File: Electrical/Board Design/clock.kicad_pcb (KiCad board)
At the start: 2 copper layers, 133.3 x 50.8 mm, 59 parts, among them CON1 AVR-ISP-6, CON2 USB-MICRO-B, IC1 ATTINY84A-SS, P1 CONN_6, P2 CONN_2, P3 CONN_2, P4 CONN_2, P5 CONN_2, P6 CONN_2, P7 CONN_2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

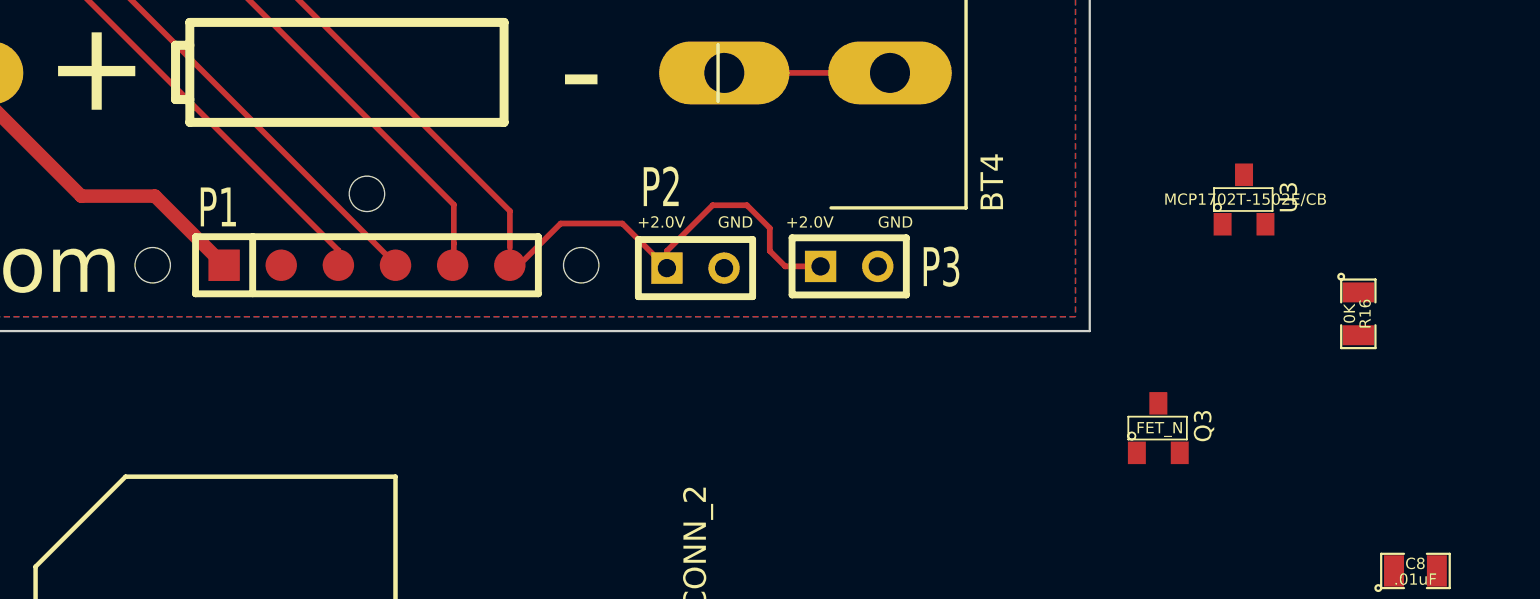
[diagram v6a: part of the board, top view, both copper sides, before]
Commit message: updated test pad foot print and also some transistors
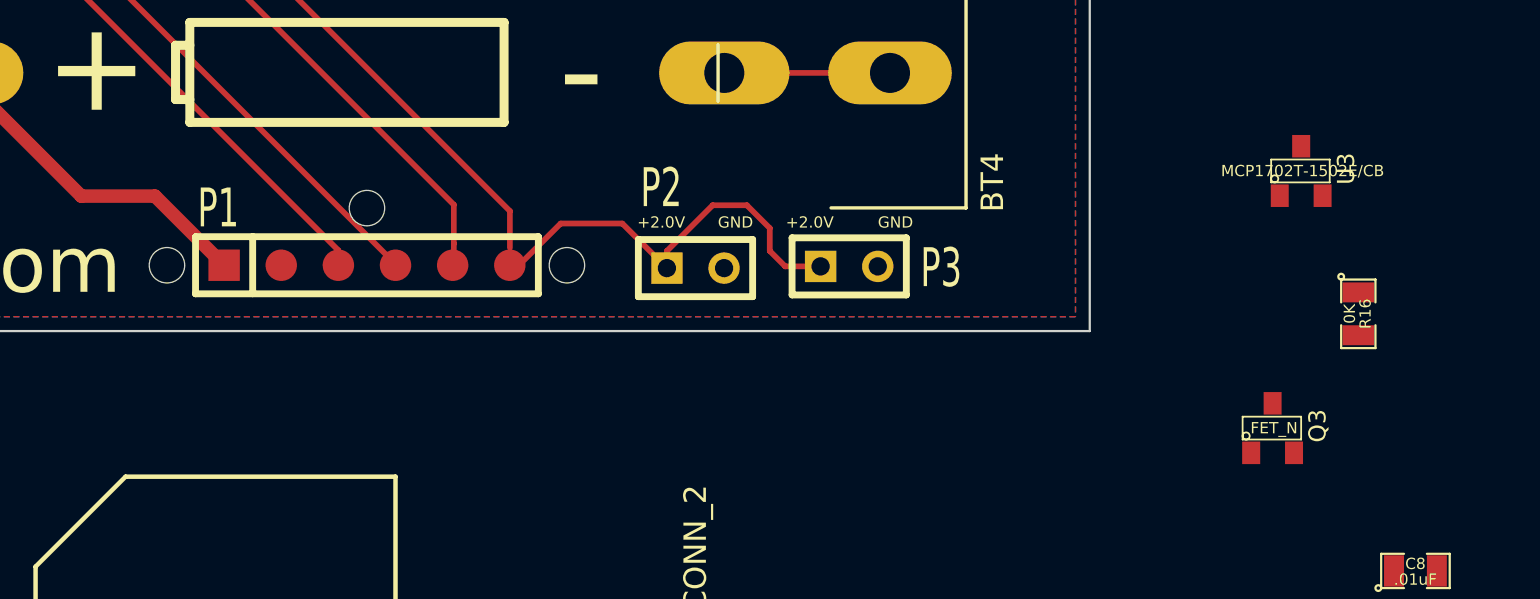
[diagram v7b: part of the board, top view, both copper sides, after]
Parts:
- moved Q3 5.08 mm to (199.4, 128.3)
- moved U3 2.84 mm to (200.7, 116.8)
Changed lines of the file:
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@@
 (kicad_pcb (version 3) (host pcbnew "(2013-07-07 BZR 4022)-stable")
   (general
-    (links 118)
-    (no_connects 40)
-    (area 57.861999 73.101999 191.312001 124.007001)
+    (links 120)
+    (no_connects 62)
+    (area 44.831088 64.333001 247.248333 153.332111)
     (thickness 1.6)
     (drawings 69)
@@
     (mod_text_size 1 1)
     (mod_text_width 0.15)
-    (pad_size 4 3)
+    (pad_size 0.8001 1.00076)
     (pad_drill 0)
     (pad_to_mask_clearance 0)
@@
     )
   )
-  (module SIL-6_s (layer F.Cu)
-    (at 159.131 121.031)
-    (descr "keyed connector")
-    (tags "CONN DEV")
-    (fp_text reference P1 (at -6.61 -2.528) (layer F.SilkS)
-      (effects (font (size 1.72974 1.08712) (thickness 0.3048)))
-    )
-    (fp_text value CONN_6 (at 3.931 -2.528) (layer F.SilkS) hide
-      (effects (font (size 1.524 1.016) (thickness 0.254)))
-    )
-    (fp_line (start -7.62 1.27) (end -7.62 -1.27) (layer F.SilkS) (width 0.3048))
-    (fp_line (start -7.62 -1.27) (end 7.62 -1.27) (layer F.SilkS) (width 0.3048))
-    (fp_line (start 7.62 -1.27) (end 7.62 1.27) (layer F.SilkS) (width 0.3048))
-    (fp_line (start 7.62 1.27) (end -7.62 1.27) (layer F.SilkS) (width 0.3048))
-    (fp_line (start -5.08 1.27) (end -5.08 -1.27) (layer F.SilkS) (width 0.3048))
-    (pad 1 smd rect (at -6.35 0) (size 1.397 1.397)
-      (layers F.Cu F.Paste F.Mask)
-      (net 5 "/BATTERY POWER")
-    )
-    (pad 2 smd circle (at -3.81 0) (size 1.397 1.397)
-      (layers F.Cu F.Paste F.Mask)
-      (net 12 GND)
-    )
-    (pad 3 smd circle (at -1.27 0) (size 1.397 1.397)
-      (layers F.Cu F.Paste F.Mask)
-      (net 9 /MINUTES)
-    )
-    (pad 4 smd circle (at 1.27 0) (size 1.397 1.397)
-      (layers F.Cu F.Paste F.Mask)
-      (net 6 /HOURS)
-    )
-    (pad 5 smd circle (at 3.81 0) (size 1.397 1.397)
-      (layers F.Cu F.Paste F.Mask)
-      (net 10 "/MODE SELECT")
-    )
-    (pad 6 smd circle (at 6.35 0) (size 1.397 1.397)
-      (layers F.Cu F.Paste F.Mask)
-      (net 31 VCC)
-    )
-    (pad "" np_thru_hole oval (at 9.525 0) (size 1.5748 1.5748) (drill 1.5748)
-      (layers *.Cu *.Mask F.SilkS)
-    )
-    (pad 1 np_thru_hole oval (at -9.525 0) (size 1.5748 1.5748) (drill 1.5748)
-      (layers *.Cu *.Mask F.SilkS)
-      (net 5 "/BATTERY POWER")
-    )
-    (pad "" np_thru_hole oval (at 0 -3.175) (size 1.5748 1.5748) (drill 1.5748)
-      (layers *.Cu *.Mask F.SilkS)
-    )
-  )
   (module bourns_knob (layer B.Cu)
     (at 67.437 80.777004)
@@
   )
   (module SOT23 (layer F.Cu)
-    (at 194.31 128.27)
+    (at 199.39 128.27)
     (tags SOT23)
     (fp_text reference Q3 (at 1.99898 -0.09906 90) (layer F.SilkS)
@@
   )
   (module SOT23 (layer F.Cu)
-    (at 198.12 118.11)
+    (at 200.66 116.84)
     (tags SOT23)
     (fp_text reference U3 (at 1.99898 -0.09906 90) (layer F.SilkS)
@@
     (fp_line (start 1.27 0.508) (end -1.3335 0.508) (layer F.SilkS) (width 0.07874))
     (fp_line (start -1.3335 -0.508) (end 1.27 -0.508) (layer F.SilkS) (width 0.07874))
-    (pad 3 smd rect (at 0 -1.09982) (size 0.8001 1.00076)
-      (layers F.Cu F.Paste F.Mask)
-    )
-    (pad 2 smd rect (at 0.9525 1.09982) (size 0.8001 1.00076)
-      (layers F.Cu F.Paste F.Mask)
-    )
-    (pad 1 smd rect (at -0.9525 1.09982) (size 0.8001 1.00076)
-      (layers F.Cu F.Paste F.Mask)
+    (pad D smd rect (at 0 -1.09982) (size 0.8001 1.00076)
+      (layers F.Cu F.Paste F.Mask)
+      (net 16 N-0000015)
+    )
+    (pad S smd rect (at 0.9525 1.09982) (size 0.8001 1.00076)
+      (layers F.Cu F.Paste F.Mask)
+      (net 12 GND)
+    )
+    (pad G smd rect (at -0.9525 1.09982) (size 0.8001 1.00076)
+      (layers F.Cu F.Paste F.Mask)
+      (net 2 "/ALARM BUZZER")
     )
     (model smd\SOT23_3.wrl
@@
     )
   )
+  (module SIL-6_s (layer F.Cu)
+    (at 159.131 121.031)
+    (descr "keyed connector")
+    (tags "CONN DEV")
+    (fp_text reference P1 (at -6.61 -2.528) (layer F.SilkS)
+      (effects (font (size 1.72974 1.08712) (thickness 0.3048)))
+    )
+    (fp_text value CONN_6 (at 3.931 -2.528) (layer F.SilkS) hide
+      (effects (font (size 1.524 1.016) (thickness 0.254)))
+    )
+    (fp_line (start -7.62 1.27) (end -7.62 -1.27) (layer F.SilkS) (width 0.3048))
+    (fp_line (start -7.62 -1.27) (end 7.62 -1.27) (layer F.SilkS) (width 0.3048))
+    (fp_line (start 7.62 -1.27) (end 7.62 1.27) (layer F.SilkS) (width 0.3048))
+    (fp_line (start 7.62 1.27) (end -7.62 1.27) (layer F.SilkS) (width 0.3048))
+    (fp_line (start -5.08 1.27) (end -5.08 -1.27) (layer F.SilkS) (width 0.3048))
+    (pad 1 smd rect (at -6.35 0) (size 1.397 1.397)
+      (layers F.Cu F.Paste F.Mask)
+      (net 5 "/BATTERY POWER")
+    )
+    (pad 2 smd circle (at -3.81 0) (size 1.397 1.397)
+      (layers F.Cu F.Paste F.Mask)
+      (net 12 GND)
+    )
+    (pad 3 smd circle (at -1.27 0) (size 1.397 1.397)
+      (layers F.Cu F.Paste F.Mask)
+      (net 9 /MINUTES)
+    )
+    (pad 4 smd circle (at 1.27 0) (size 1.397 1.397)
+      (layers F.Cu F.Paste F.Mask)
+      (net 6 /HOURS)
+    )
+    (pad 5 smd circle (at 3.81 0) (size 1.397 1.397)
+      (layers F.Cu F.Paste F.Mask)
+      (net 10 "/MODE SELECT")
+    )
+    (pad 6 smd circle (at 6.35 0) (size 1.397 1.397)
+      (layers F.Cu F.Paste F.Mask)
+      (net 31 VCC)
+    )
+    (pad "" np_thru_hole oval (at 8.89 0) (size 1.5748 1.5748) (drill 1.5748)
+      (layers *.Cu *.Mask F.SilkS)
+    )
+    (pad "" np_thru_hole oval (at -8.89 0) (size 1.5748 1.5748) (drill 1.5748)
+      (layers *.Cu *.Mask F.SilkS)
+    )
+    (pad "" np_thru_hole oval (at 0 -2.54) (size 1.5748 1.5748) (drill 1.5748)
+      (layers *.Cu *.Mask F.SilkS)
+    )
+  )

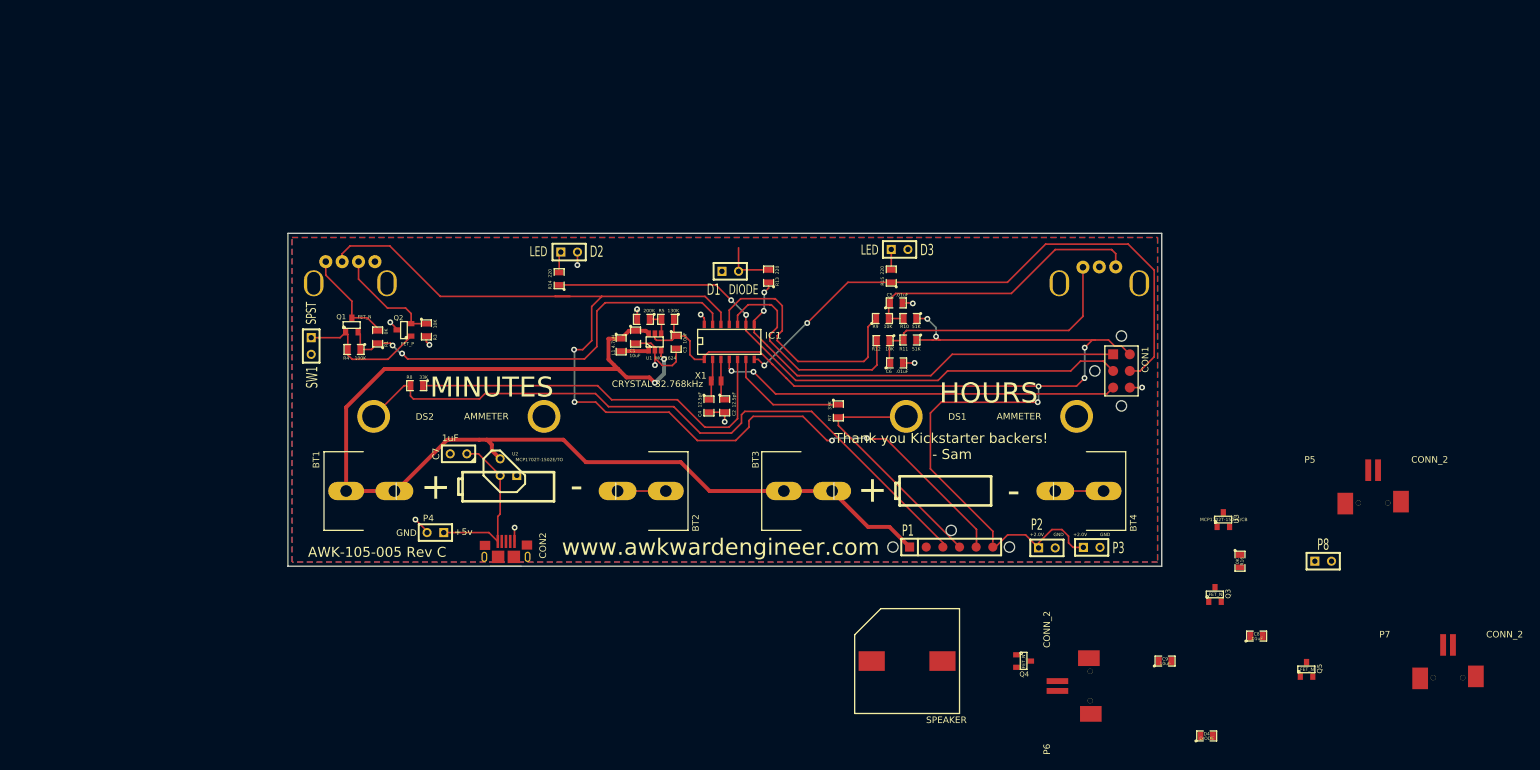
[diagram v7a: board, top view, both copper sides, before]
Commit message: reorganized board layout, but haven't fully wired
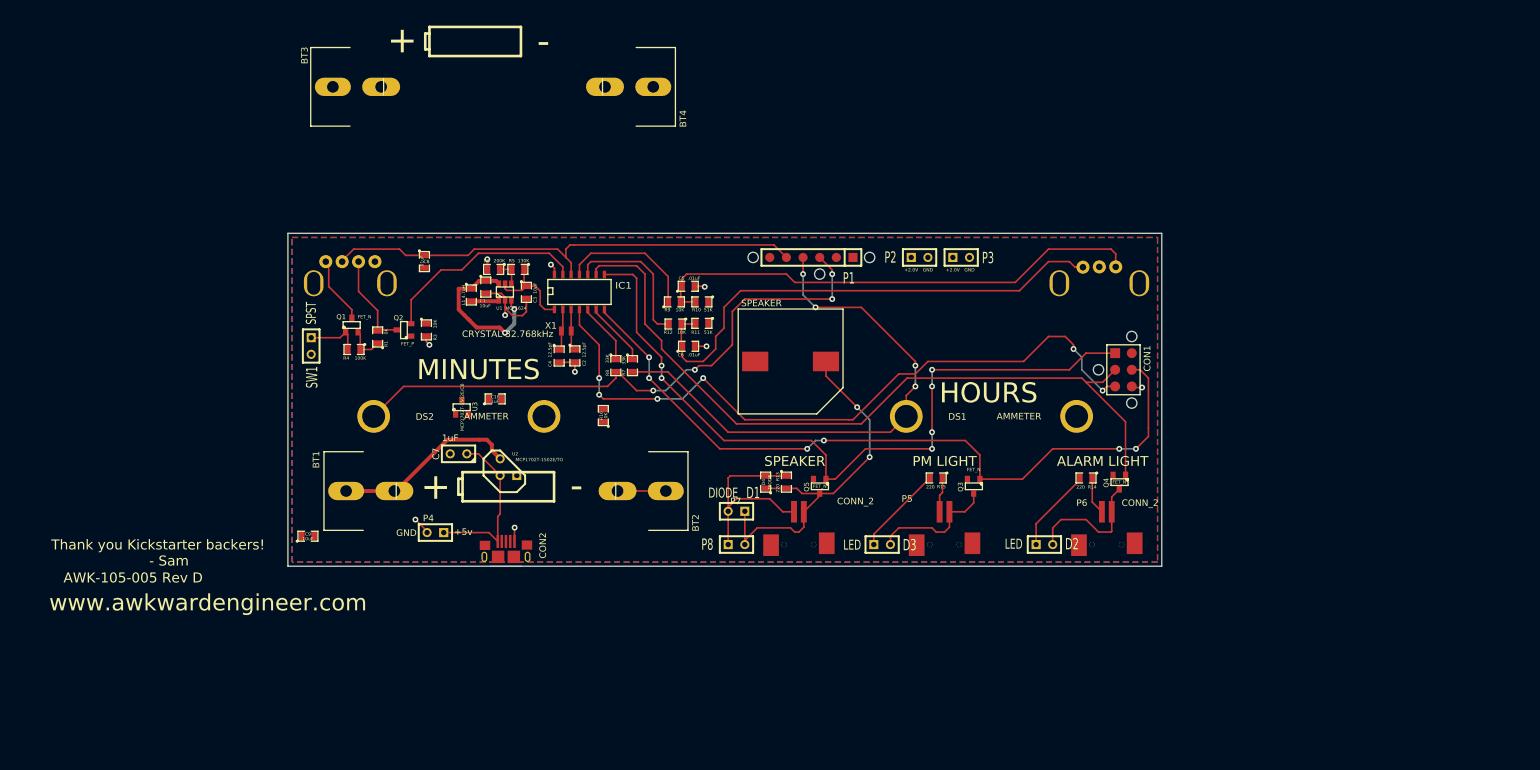
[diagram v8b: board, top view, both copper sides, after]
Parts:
- added C10: 1uF, SM0805, F.Cu at (89.5, 98.4)
- moved C8 139.3 mm to (78.7, 77.5), turned to 270 degrees
- moved C9 132.2 mm to (61.0, 119.4)
- moved U3 117.5 mm to (84.5, 99.7)
- moved P7 101.1 mm to (135.9, 120.7)
- moved R16 99.7 mm to (106.0, 101.0), turned to 90 degrees
- moved BT3 92.4 mm to (72.4, 50.8)
- moved BT4 92.3 mm to (106.0, 50.8)
- moved P8 89.6 mm to (126.4, 120.7)
- moved R14 86.0 mm to (179.7, 110.5), turned to 180 degrees
- moved D2 85.2 mm to (173.4, 120.7)
- moved Q5 79.4 mm to (139.1, 111.8), turned to 180 degrees
- moved D4 77.7 mm to (130.8, 111.1), turned to 90 degrees
- moved P5 65.7 mm to (158.1, 120.7)
- moved P1 49.1 mm to (137.8, 76.8), turned to 180 degrees
- moved SP1 49.1 mm to (134.6, 92.7), turned to 0 degrees
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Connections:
- Q1 pad D: N-0000018 -> N-0000015
- R2 pad 1: N-0000016 -> N-0000015
- R2 pad 3: N-0000018 -> N-0000016
- R3 pad 1: N-0000018 -> N-0000015
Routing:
- net VCC: track 183.4 -> 14.1 mm, vias 6 -> 0
- net /BATTERY POWER: track 180.8 -> 52.8 mm
- net /MODE SELECT: track 162.6 -> 75.3 mm, vias 4 -> 0
- net N-000008: track 0.00 -> 58.1 mm, vias 0 -> 2
- net /ALARM BUZZER: track 60.7 -> 114.7 mm, vias 0 -> 6
- net /ALARM LIGHT: track 63.4 -> 116.1 mm
- net N-000009: track 60.2 -> 9.39 mm
- net /AM PM LIGHT: track 64.2 -> 113.7 mm, vias 2 -> 6
- net N-000005: track 62.0 -> 107.6 mm, vias 2 -> 6
- net /HOURS: track 37.9 -> 82.6 mm, vias 0 -> 4
- net /MODE SELECT POWER: track 78.3 -> 34.8 mm, vias 2 -> 0
- net N-0000025: track 42.6 -> 78.4 mm
- net N-0000010: track 45.2 -> 77.3 mm
- net N-0000026: track 0.00 -> 19.4 mm
- net N-0000029: track 24.3 -> 5.34 mm
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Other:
- board text added: "ALARM LIGHT"
- board text added: "AWK-105-005 Rev D"
- board text added: "PM LIGHT"
- board text added: "SPEAKER"
- board text removed: "AWK-105-005 Rev C"
